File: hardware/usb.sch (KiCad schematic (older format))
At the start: 2 parts

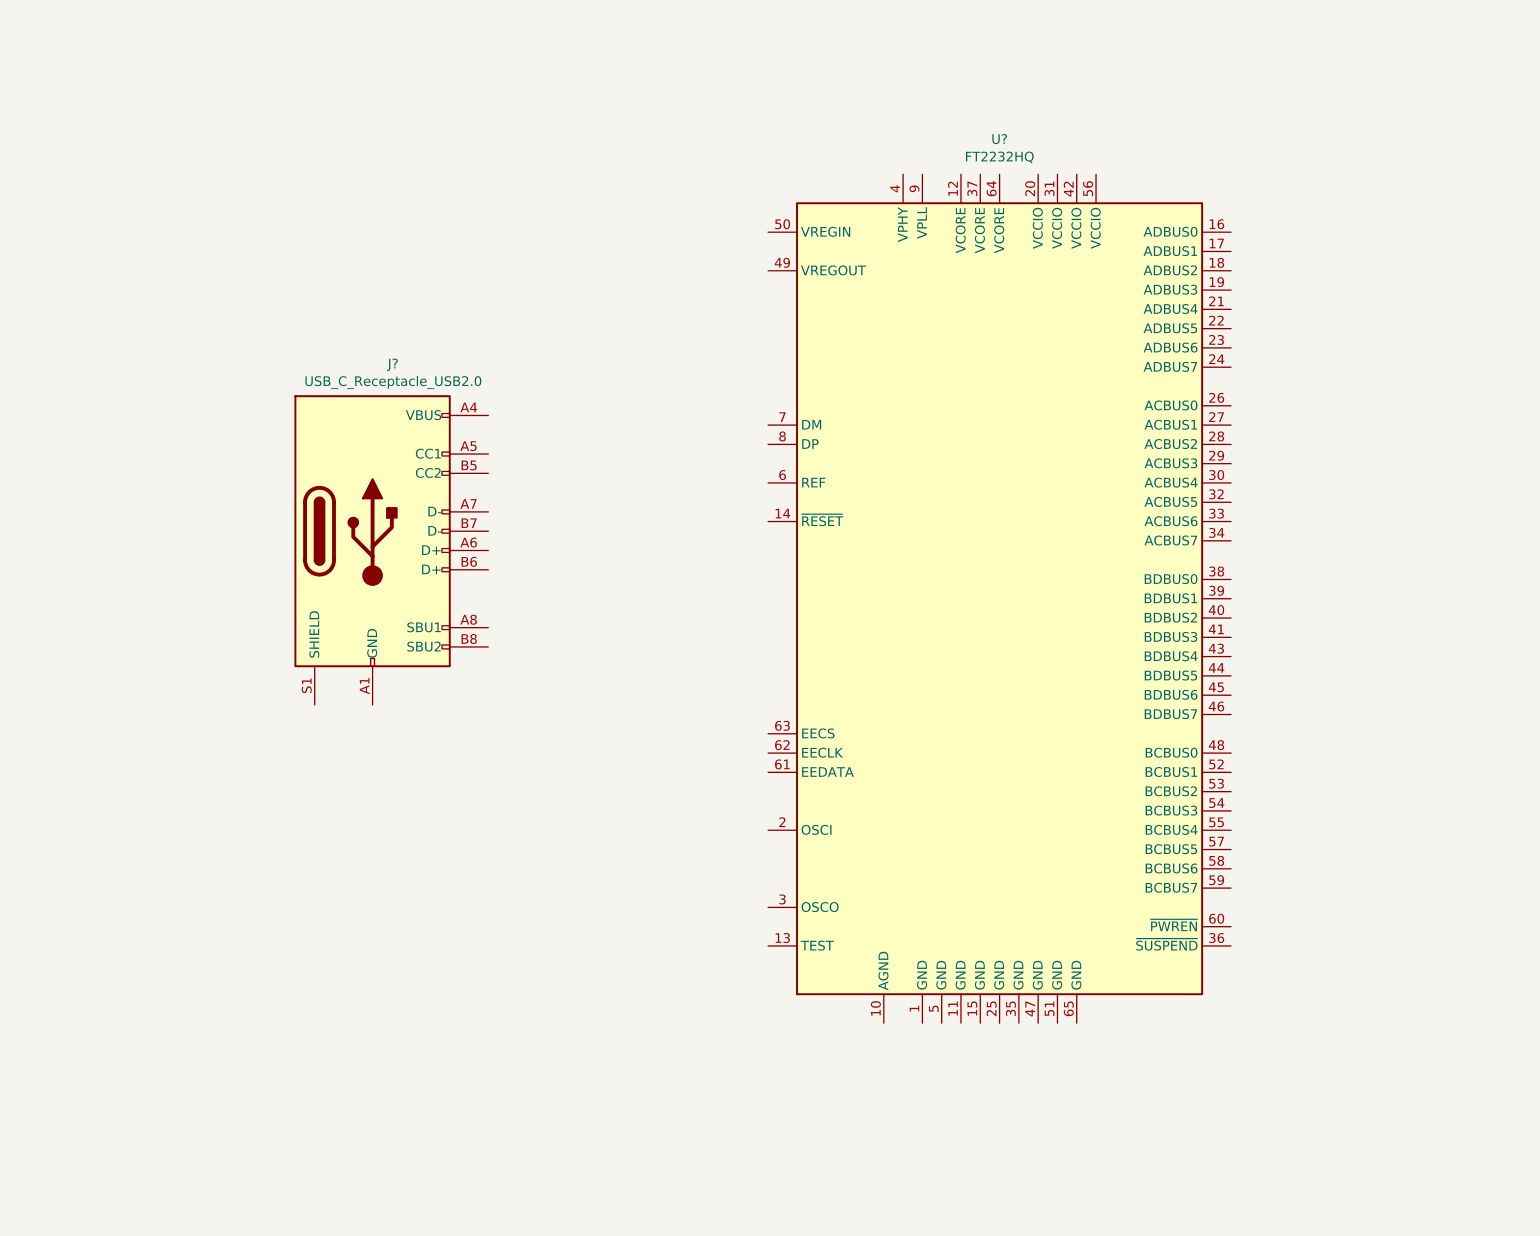
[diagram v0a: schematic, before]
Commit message: Finish FTDI schematic, add datasheets
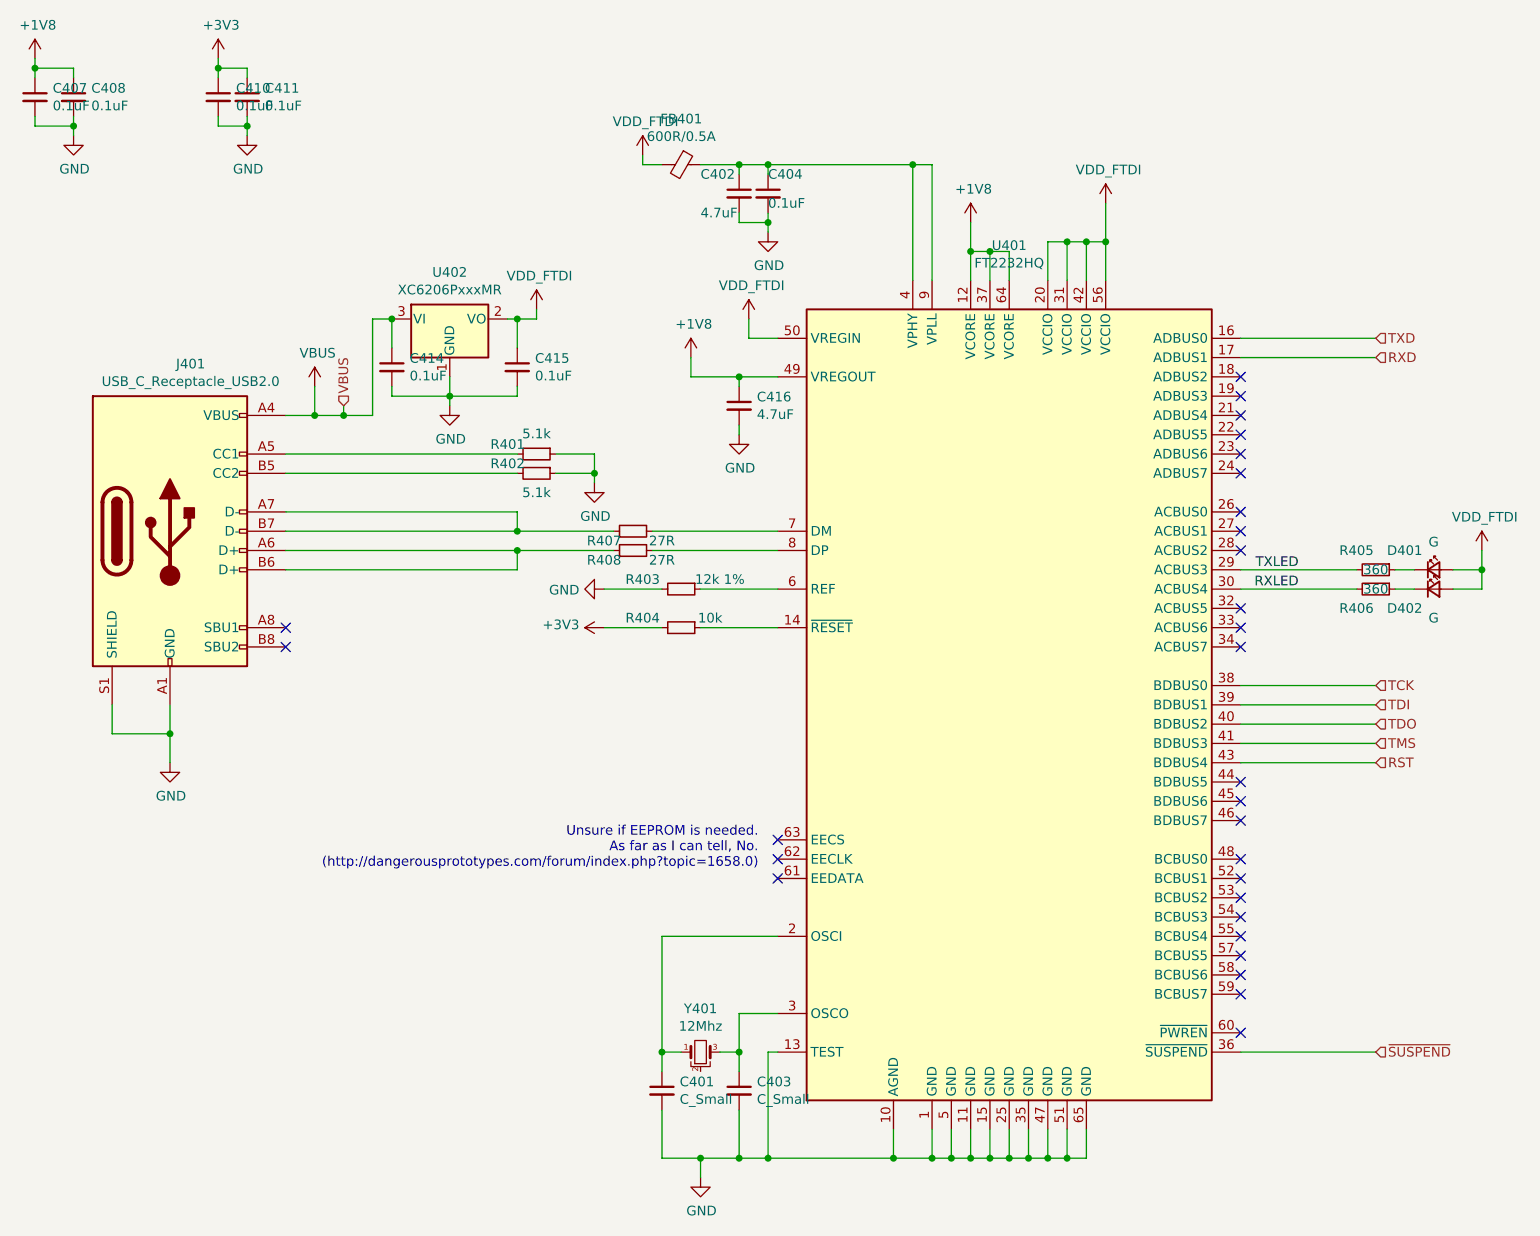
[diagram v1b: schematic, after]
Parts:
- added C401, C403: C_Small, symbol Device:C_Small
- added C402, C416: 4.7uF, symbol Device:C_Small
- added C404, C407, C408, C410, C411, C414, C415: 0.1uF, symbol Device:C_Small
- added D401, D402: G, symbol Device:LED_Small
- added FB401: 600R/0.5A, symbol Device:Ferrite_Bead_Small
- added R401, R402: 5.1k, symbol Device:R_Small
- added R403: 12k 1%, symbol Device:R_Small
- added R404: 10k, symbol Device:R_Small
- added R405, R406: 360, symbol Device:R_Small
- added R407, R408: 27R, symbol Device:R_Small
- added U402: XC6206PxxxMR, Package_TO_SOT_SMD:SOT-23, symbol Regulator_Linear:XC6206PxxxMR
- added Y401: 12Mhz, symbol Device:Crystal_GND2_Small
- gave numbers to parts that had none: 2
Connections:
- net GND: now reaches J401.A1 (GND), J401.A12 (GND), J401.B1 (GND), J401.B12 (GND)
- net GND: now also J401.S1 (SHIELD), U401.1 (GND), U401.10 (AGND), U401.11 (GND), U401.13 (TEST), U401.15 (GND), U401.25 (GND), U401.35 (GND), U401.47 (GND), U401.5 (GND), U401.51 (GND), U401.65 (GND), C401.2, C402.2, C403.2, C404.2, C407.2, C408.2, C410.2, C411.2, C414.2, C415.2, C416.2, R401.1, R402.1, R403.2, U402.1 (GND)
- net VBUS: now reaches J401.A4 (VBUS), J401.A9 (VBUS), J401.B4 (VBUS), J401.B9 (VBUS)
- net VBUS: now also C414.1, U402.3 (VI)
- net at J401.A5 (CC1): now also R401.2
- net at J401.A6 (D+): now also J401.B6 (D+), R408.1
- net at J401.A7 (D-): now also J401.B7 (D-), R407.1
- net at J401.B5 (CC2): now also R402.2
- net +1V8: now reaches U401.12 (VCORE)
- net +1V8: now also U401.37 (VCORE), U401.49 (VREGOUT), U401.64 (VCORE), C407.1, C408.1, C416.1
- net at U401.14 (~RESET): now also R404.1
- net TXD: now reaches U401.16 (ADBUS0)
- net RXD: now reaches U401.17 (ADBUS1)
- net at U401.2 (OSCI): now also C401.1, Y401.1
- net VDD_FTDI: now reaches U401.20 (VCCIO)
- net VDD_FTDI: now also U401.31 (VCCIO), U401.42 (VCCIO), U401.50 (VREGIN), U401.56 (VCCIO), C415.1, D401.2 (A), D402.2 (A), FB401.2, U402.2 (VO)
- net TXLED: now reaches U401.29 (ACBUS3)
- net TXLED: now also R405.2
- net at U401.3 (OSCO): now also C403.1, Y401.3
- net RXLED: now reaches U401.30 (ACBUS4)
- net RXLED: now also R406.2
- net ~SUSPEND~: now reaches U401.36 (~SUSPEND)
- net TCK: now reaches U401.38 (BDBUS0)
- net TDI: now reaches U401.39 (BDBUS1)
- net at U401.4 (VPHY): now also U401.9 (VPLL), C402.1, C404.1, FB401.1
- net TDO: now reaches U401.40 (BDBUS2)
- net TMS: now reaches U401.41 (BDBUS3)
- net RST: now reaches U401.43 (BDBUS4)
- net at U401.6 (REF): now also R403.1
- net at U401.7 (DM): now also R407.2
- net at U401.8 (DP): now also R408.2
- new net: D402.1 (K), R406.1
- new net: D401.1 (K), R405.1
- new net +3V3: C410.1, C411.1, R404.2
- no-connect marks 0 -> 29
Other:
- note added: "Unsure if EEPROM is needed.\nAs far as I can tell, No.\n(http://dangerousprototypes.com/forum/index.php?topic=1658.0)"
- moved on the sheet: J401, U401

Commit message: More stuff
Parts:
- C401, C402, C403, C404, C407, C408, C410, C411, C414, C415, C416: footprint (none) -> Capacitor_SMD:C_0603_1608Metric
- D401, D402: footprint (none) -> LED_SMD:LED_0603_1608Metric
- J401: footprint (none) -> Connector_USB:USB_C_Receptacle_GCT_USB4085
- R401, R402, R403, R404, R405, R406, R407, R408: footprint (none) -> Resistor_SMD:R_0603_1608Metric
- Y401: footprint (none) -> Crystal:Crystal_HC35-U
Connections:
- net CC1: now reaches J401.A5 (CC1), R401.2
- net CC2: now reaches J401.B5 (CC2), R402.2
- net REF: now reaches R403.1, U401.6 (REF)
- net ~RESET~: now reaches R404.1, U401.14 (~RESET)
- net D+: now reaches J401.A6 (D+), J401.B6 (D+), R408.1
- net D-: now reaches J401.A7 (D-), J401.B7 (D-), R407.1
- net OSCI: now reaches C401.1, U401.2 (OSCI), Y401.1
- net OSCO: now reaches C403.1, U401.3 (OSCO), Y401.3
- net VPHY: now reaches C402.1, C404.1, FB401.1, U401.4 (VPHY), U401.9 (VPLL)
- net FTDI_D-: now reaches R407.2, U401.7 (DM)
- net FTDI_D+: now reaches R408.2, U401.8 (DP)
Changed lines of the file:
@@
 F 0 "J401" H 1907 4267 50  0000 C CNN
 F 1 "USB_C_Receptacle_USB2.0" H 1907 4176 50  0000 C CNN
-F 2 "" H 1950 3400 50  0001 C CNN
+F 2 "Connector_USB:USB_C_Receptacle_GCT_USB4085" H 1950 3400 50  0001 C CNN
 F 3 "https://www.usb.org/sites/default/files/documents/usb_type-c.zip" H 1950 3400 50  0001 C CNN
 	1    1800 3400
@@
 F 0 "R401" V 3650 2850 50  0000 C CNN
 F 1 "5.1k" V 3595 3000 50  0000 C CNN
-F 2 "" H 3700 3000 50  0001 C CNN
+F 2 "Resistor_SMD:R_0603_1608Metric" H 3700 3000 50  0001 C CNN
 F 3 "~" H 3700 3000 50  0001 C CNN
 	1    3700 3000
@@
 F 0 "R402" V 3650 2950 50  0000 C CNN
 F 1 "5.1k" V 3800 3100 50  0000 C CNN
-F 2 "" H 3700 3100 50  0001 C CNN
+F 2 "Resistor_SMD:R_0603_1608Metric" H 3700 3100 50  0001 C CNN
 F 3 "~" H 3700 3100 50  0001 C CNN
 	1    3700 3100
@@
 F 0 "R404" V 4400 3700 50  0000 C CNN
 F 1 "10k" V 4400 4050 50  0000 C CNN
-F 2 "" H 4450 3900 50  0001 C CNN
+F 2 "Resistor_SMD:R_0603_1608Metric" H 4450 3900 50  0001 C CNN
 F 3 "~" H 4450 3900 50  0001 C CNN
 	1    4450 3900
@@
 F 0 "R403" V 4400 3500 50  0000 C CNN
 F 1 "12k 1%" V 4400 3900 50  0000 C CNN
-F 2 "" H 4450 3700 50  0001 C CNN
+F 2 "Resistor_SMD:R_0603_1608Metric" H 4450 3700 50  0001 C CNN
 F 3 "~" H 4450 3700 50  0001 C CNN
 	1    4450 3700
@@
 F 0 "Y401" H 4550 6325 50  0000 C CNN
 F 1 "12Mhz" H 4550 6234 50  0000 C CNN
-F 2 "" H 4550 6100 50  0001 C CNN
+F 2 "Crystal:Crystal_HC35-U" H 4550 6100 50  0001 C CNN
 F 3 "~" H 4550 6100 50  0001 C CNN
 	1    4550 6100
@@
 F 0 "C401" H 4442 6346 50  0000 L CNN
 F 1 "C_Small" H 4442 6255 50  0000 L CNN
-F 2 "" H 4350 6300 50  0001 C CNN
+F 2 "Capacitor_SMD:C_0603_1608Metric" H 4350 6300 50  0001 C CNN
 F 3 "~" H 4350 6300 50  0001 C CNN
 	1    4350 6300
@@
 F 0 "C403" H 4842 6346 50  0000 L CNN
 F 1 "C_Small" H 4842 6255 50  0000 L CNN
-F 2 "" H 4750 6300 50  0001 C CNN
+F 2 "Capacitor_SMD:C_0603_1608Metric" H 4750 6300 50  0001 C CNN
 F 3 "~" H 4750 6300 50  0001 C CNN
 	1    4750 6300
@@
 F 0 "D402" H 8200 3600 50  0000 C CNN
 F 1 "G" H 8350 3550 50  0000 C CNN
-F 2 "" V 8350 3700 50  0001 C CNN
+F 2 "LED_SMD:LED_0603_1608Metric" V 8350 3700 50  0001 C CNN
 F 3 "~" V 8350 3700 50  0001 C CNN
 	1    8350 3700
@@
 F 0 "D401" H 8200 3700 50  0000 C CNN
 F 1 "G" H 8350 3744 50  0000 C CNN
-F 2 "" V 8350 3600 50  0001 C CNN
+F 2 "LED_SMD:LED_0603_1608Metric" V 8350 3600 50  0001 C CNN
 F 3 "~" V 8350 3600 50  0001 C CNN
 	1    8350 3600
@@
 F 0 "R405" V 7950 3500 50  0000 C CNN
 F 1 "360" V 8050 3600 50  0000 C CNN
-F 2 "" H 8050 3600 50  0001 C CNN
+F 2 "Resistor_SMD:R_0603_1608Metric" H 8050 3600 50  0001 C CNN
 F 3 "~" H 8050 3600 50  0001 C CNN
 	1    8050 3600
@@
 F 0 "R406" V 8150 3600 50  0000 C CNN
 F 1 "360" V 8050 3700 50  0000 C CNN
-F 2 "" H 8050 3700 50  0001 C CNN
+F 2 "Resistor_SMD:R_0603_1608Metric" H 8050 3700 50  0001 C CNN
 F 3 "~" H 8050 3700 50  0001 C CNN
 	1    8050 3700
@@
 F 0 "C402" H 4550 1750 50  0000 L CNN
 F 1 "4.7uF" H 4550 1550 50  0000 L CNN
-F 2 "" H 4750 1650 50  0001 C CNN
+F 2 "Capacitor_SMD:C_0603_1608Metric" H 4750 1650 50  0001 C CNN
 F 3 "~" H 4750 1650 50  0001 C CNN
 	1    4750 1650
@@
 F 0 "C404" H 4900 1750 50  0000 L CNN
 F 1 "0.1uF" H 4900 1600 50  0000 L CNN
-F 2 "" H 4900 1650 50  0001 C CNN
+F 2 "Capacitor_SMD:C_0603_1608Metric" H 4900 1650 50  0001 C CNN
 F 3 "~" H 4900 1650 50  0001 C CNN
 	1    4900 1650
@@
 F 0 "C416" H 4842 2796 50  0000 L CNN
 F 1 "4.7uF" H 4842 2705 50  0000 L CNN
-F 2 "" H 4750 2750 50  0001 C CNN
+F 2 "Capacitor_SMD:C_0603_1608Metric" H 4750 2750 50  0001 C CNN
 F 3 "~" H 4750 2750 50  0001 C CNN
 	1    4750 2750
@@
 F 0 "C407" H 1192 1196 50  0000 L CNN
 F 1 "0.1uF" H 1192 1105 50  0000 L CNN
-F 2 "" H 1100 1150 50  0001 C CNN
+F 2 "Capacitor_SMD:C_0603_1608Metric" H 1100 1150 50  0001 C CNN
 F 3 "~" H 1100 1150 50  0001 C CNN
 	1    1100 1150
@@
 F 0 "C408" H 1392 1196 50  0000 L CNN
 F 1 "0.1uF" H 1392 1105 50  0000 L CNN
-F 2 "" H 1300 1150 50  0001 C CNN
+F 2 "Capacitor_SMD:C_0603_1608Metric" H 1300 1150 50  0001 C CNN
 F 3 "~" H 1300 1150 50  0001 C CNN
 	1    1300 1150
@@
 F 0 "C410" H 2142 1196 50  0000 L CNN
 F 1 "0.1uF" H 2142 1105 50  0000 L CNN
-F 2 "" H 2050 1150 50  0001 C CNN
+F 2 "Capacitor_SMD:C_0603_1608Metric" H 2050 1150 50  0001 C CNN
 F 3 "~" H 2050 1150 50  0001 C CNN
 	1    2050 1150
@@
 F 0 "C411" H 2292 1196 50  0000 L CNN
 F 1 "0.1uF" H 2292 1105 50  0000 L CNN
-F 2 "" H 2200 1150 50  0001 C CNN
+F 2 "Capacitor_SMD:C_0603_1608Metric" H 2200 1150 50  0001 C CNN
 F 3 "~" H 2200 1150 50  0001 C CNN
 	1    2200 1150
@@
 F 0 "R407" V 4150 3550 50  0000 C CNN
 F 1 "27R" V 4150 3250 50  0000 C CNN
-F 2 "" H 4200 3400 50  0001 C CNN
+F 2 "Resistor_SMD:R_0603_1608Metric" H 4200 3400 50  0001 C CNN
 F 3 "~" H 4200 3400 50  0001 C CNN
 	1    4200 3400
@@
 F 0 "R408" V 4150 3650 50  0000 C CNN
 F 1 "27R" V 4150 3350 50  0000 C CNN
-F 2 "" H 4200 3500 50  0001 C CNN
+F 2 "Resistor_SMD:R_0603_1608Metric" H 4200 3500 50  0001 C CNN
 F 3 "~" H 4200 3500 50  0001 C CNN
 	1    4200 3500
@@
 F 0 "C414" H 3042 2596 50  0000 L CNN
 F 1 "0.1uF" H 3042 2505 50  0000 L CNN
-F 2 "" H 2950 2550 50  0001 C CNN
+F 2 "Capacitor_SMD:C_0603_1608Metric" H 2950 2550 50  0001 C CNN
 F 3 "~" H 2950 2550 50  0001 C CNN
 	1    2950 2550
@@
 F 0 "C415" H 3692 2596 50  0000 L CNN
 F 1 "0.1uF" H 3692 2505 50  0000 L CNN
-F 2 "" H 3600 2550 50  0001 C CNN
+F 2 "Capacitor_SMD:C_0603_1608Metric" H 3600 2550 50  0001 C CNN
 F 3 "~" H 3600 2550 50  0001 C CNN
 	1    3600 2550
@@
 	1300 1300 1300 1350
 Connection ~ 1300 1300
+Text Label 2500 3300 0    50   ~ 0
+D-
+Text Label 2500 3500 0    50   ~ 0
+D+
+Text Label 4500 3400 0    50   ~ 0
+FTDI_D-
+Text Label 4500 3500 0    50   ~ 0
+FTDI_D+
+Text Label 4700 3900 0    50   ~ 0
+~RESET~
+Text Label 2700 3000 0    50   ~ 0
+CC1
+Text Label 2700 3100 0    50   ~ 0
+CC2
+Text Label 4600 5500 0    50   ~ 0
+OSCI
+Text Label 4800 5900 0    50   ~ 0
+OSCO
+Text Label 4750 3700 0    50   ~ 0
+REF
+Text Label 5650 1950 1    50   ~ 0
+VPHY
 $EndSCHEMATC
